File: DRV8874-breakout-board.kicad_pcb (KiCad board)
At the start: 2 copper layers, 27 x 40 mm, 17 parts, among them J101 M0_CONN, J102 Conn_01x02_Pin, J103 M0_CONN, J104 Conn_01x06_Pin, J105 PMODE

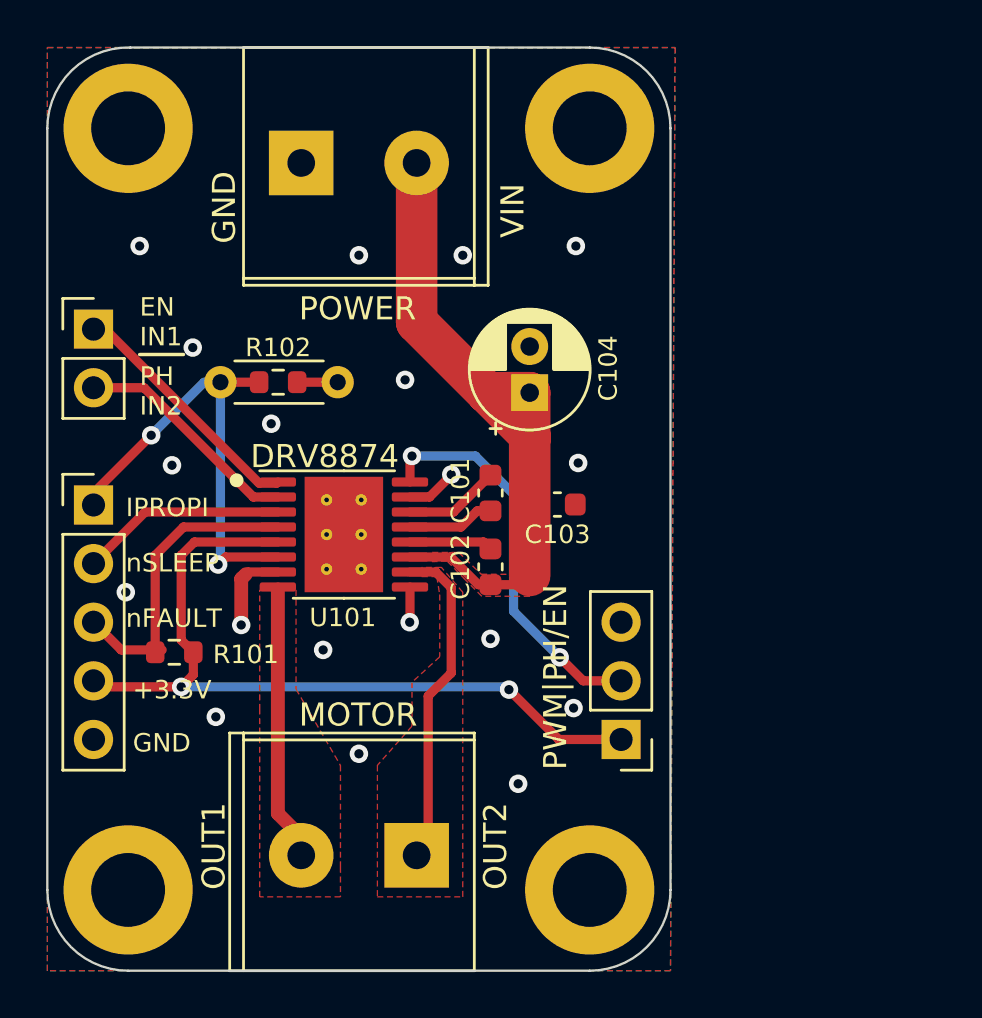
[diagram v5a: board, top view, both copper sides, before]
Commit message: Update screw terminal
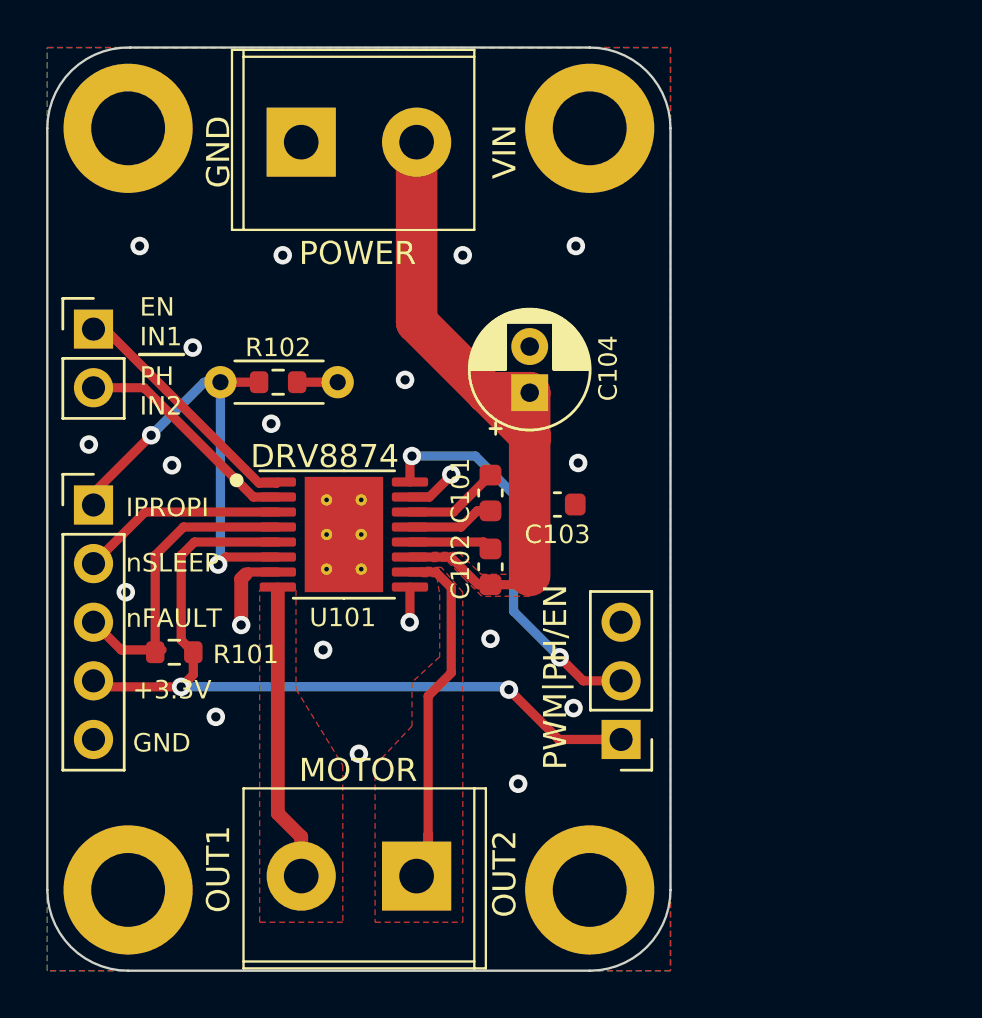
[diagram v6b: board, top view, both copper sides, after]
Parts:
- J101, J103: footprint VsReality_Footprints:Ningbo_Kangnex_Elec_WJ128V_5_0_2P -> VsReality_Footprints:JILN JL126-50002G01
- moved J103 0.90 mm to (130.6, 79.8)
- moved J101 0.90 mm to (130.6, 111.6)
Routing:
- net OUT2: track 14.3 -> 16.3 mm
- net OUT1: track 12.4 -> 14.1 mm
- net VMOTORS: track 29.8 -> 30.7 mm
- net GND: vias 19 -> 20
